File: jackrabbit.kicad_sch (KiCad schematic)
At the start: 55 parts, among them J1 USB_C, J2 PinHeader_2.54mm_02x08, J3 PinHeader_2.54mm_02x08, J4 PinHeader_2.54mm_02x04, J5 PinHeader_2.54mm_02x04, J6 PinHeader_2.54mm_01x04, J7 PinHeader_2.54mm_01x03, SW1 SW_Push, SW2 SW_Push, U1 MIC5319-3.3YD5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

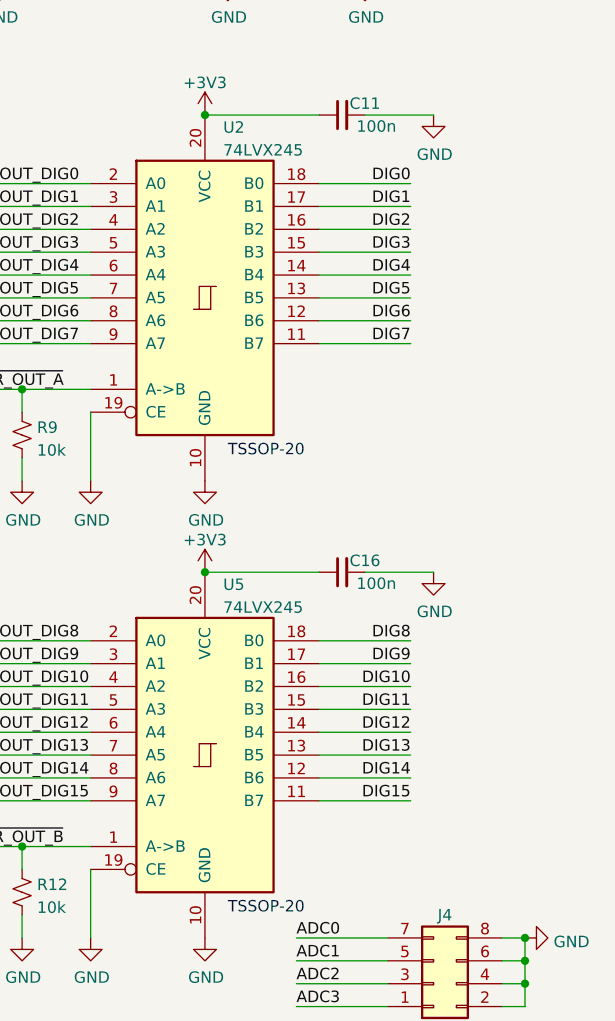
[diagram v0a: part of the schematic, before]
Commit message: Add bus contention series protection resistors
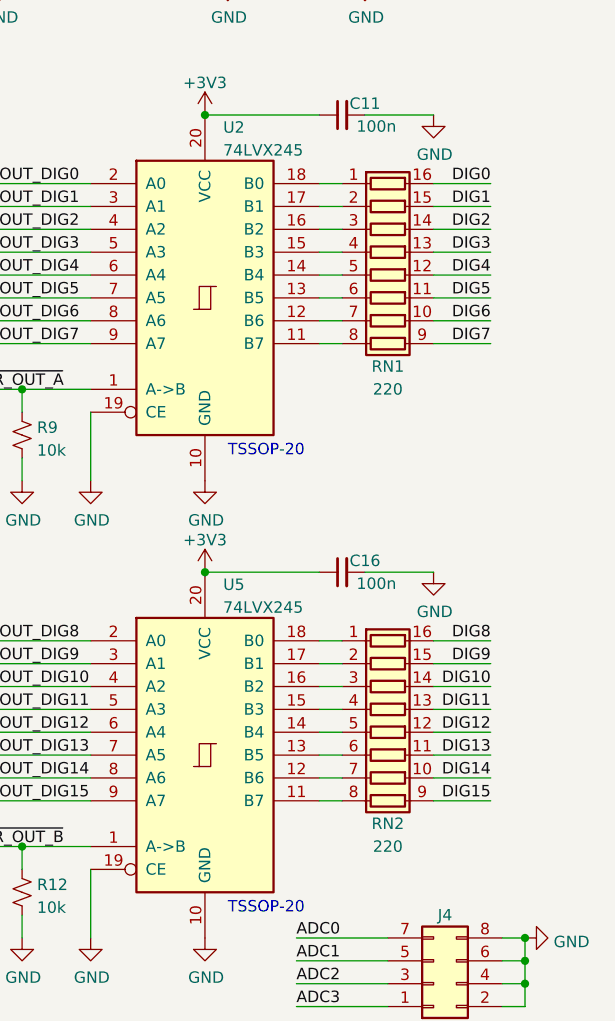
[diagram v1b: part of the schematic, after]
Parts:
- added RN1, RN2: 220, Resistor_SMD:R_Array_Convex_8x0602, symbol Device:R_Pack08
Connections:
- net DIG0: now also RN1.16 (R1.2); no longer U2.18 (B0)
- net DIG1: now also RN1.15 (R2.2); no longer U2.17 (B1)
- net DIG10: now also RN2.14 (R3.2); no longer U5.16 (B2)
- net DIG11: now also RN2.13 (R4.2); no longer U5.15 (B3)
- net DIG12: now also RN2.12 (R5.2); no longer U5.14 (B4)
- net DIG13: now also RN2.11 (R6.2); no longer U5.13 (B5)
- net DIG14: now also RN2.10 (R7.2); no longer U5.12 (B6)
- net DIG15: now also RN2.9 (R8.2); no longer U5.11 (B7)
- net DIG2: now also RN1.14 (R3.2); no longer U2.16 (B2)
- net DIG3: now also RN1.13 (R4.2); no longer U2.15 (B3)
- net DIG4: now also RN1.12 (R5.2); no longer U2.14 (B4)
- net DIG5: now also RN1.11 (R6.2); no longer U2.13 (B5)
- net DIG6: now also RN1.10 (R7.2); no longer U2.12 (B6)
- net DIG7: now also RN1.9 (R8.2); no longer U2.11 (B7)
- net DIG8: now also RN2.16 (R1.2); no longer U5.18 (B0)
- net DIG9: now also RN2.15 (R2.2); no longer U5.17 (B1)
- new net: RN1.8 (R8.1), U2.11 (B7)
- new net: RN1.7 (R7.1), U2.12 (B6)
- new net: RN1.6 (R6.1), U2.13 (B5)
- new net: RN1.5 (R5.1), U2.14 (B4)
- new net: RN1.4 (R4.1), U2.15 (B3)
- new net: RN1.3 (R3.1), U2.16 (B2)
- new net: RN1.2 (R2.1), U2.17 (B1)
- new net: RN1.1 (R1.1), U2.18 (B0)
- new net: RN2.8 (R8.1), U5.11 (B7)
- new net: RN2.7 (R7.1), U5.12 (B6)
- new net: RN2.6 (R6.1), U5.13 (B5)
- new net: RN2.5 (R5.1), U5.14 (B4)
- new net: RN2.4 (R4.1), U5.15 (B3)
- new net: RN2.3 (R3.1), U5.16 (B2)
- new net: RN2.2 (R2.1), U5.17 (B1)
- new net: RN2.1 (R1.1), U5.18 (B0)

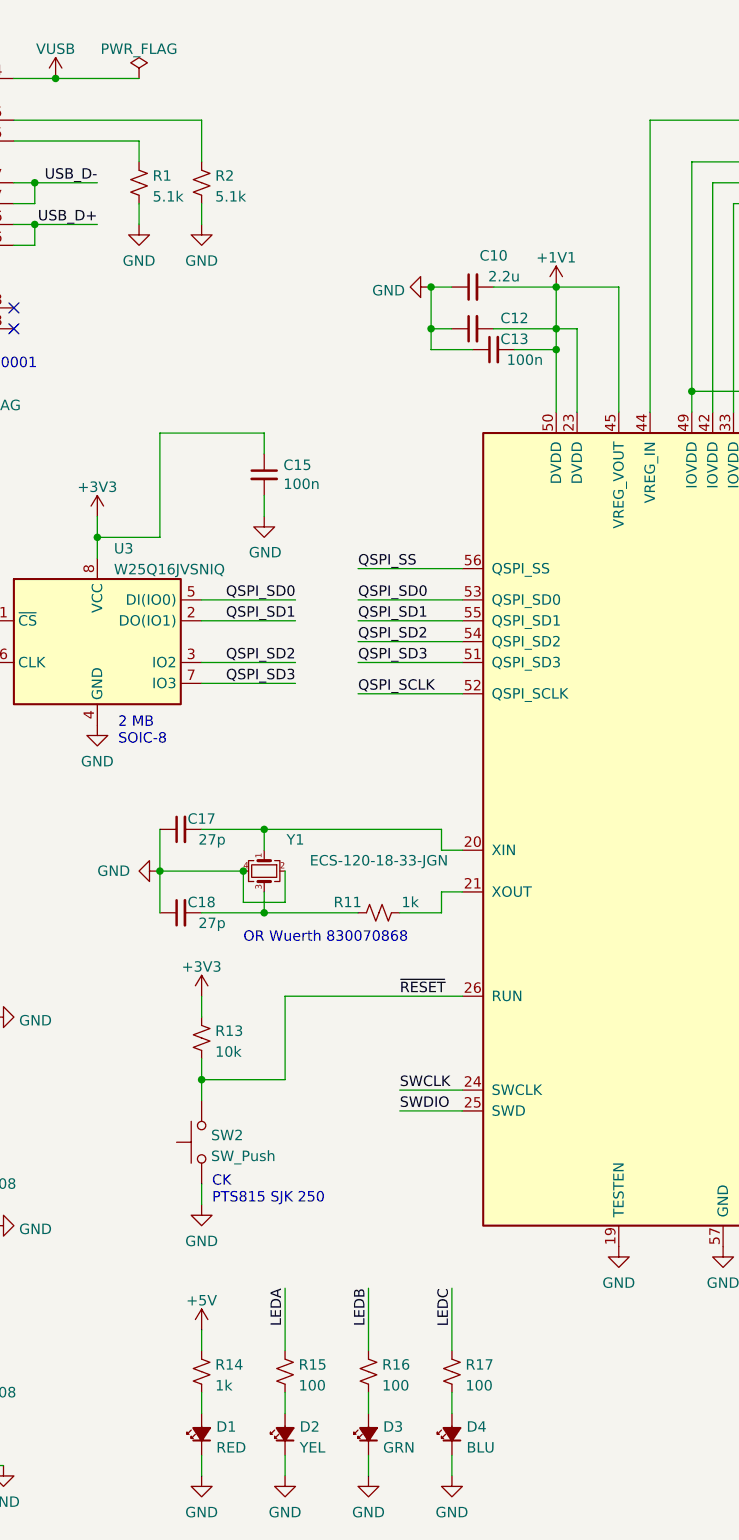
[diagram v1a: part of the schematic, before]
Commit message: Start layout with passives on bottom
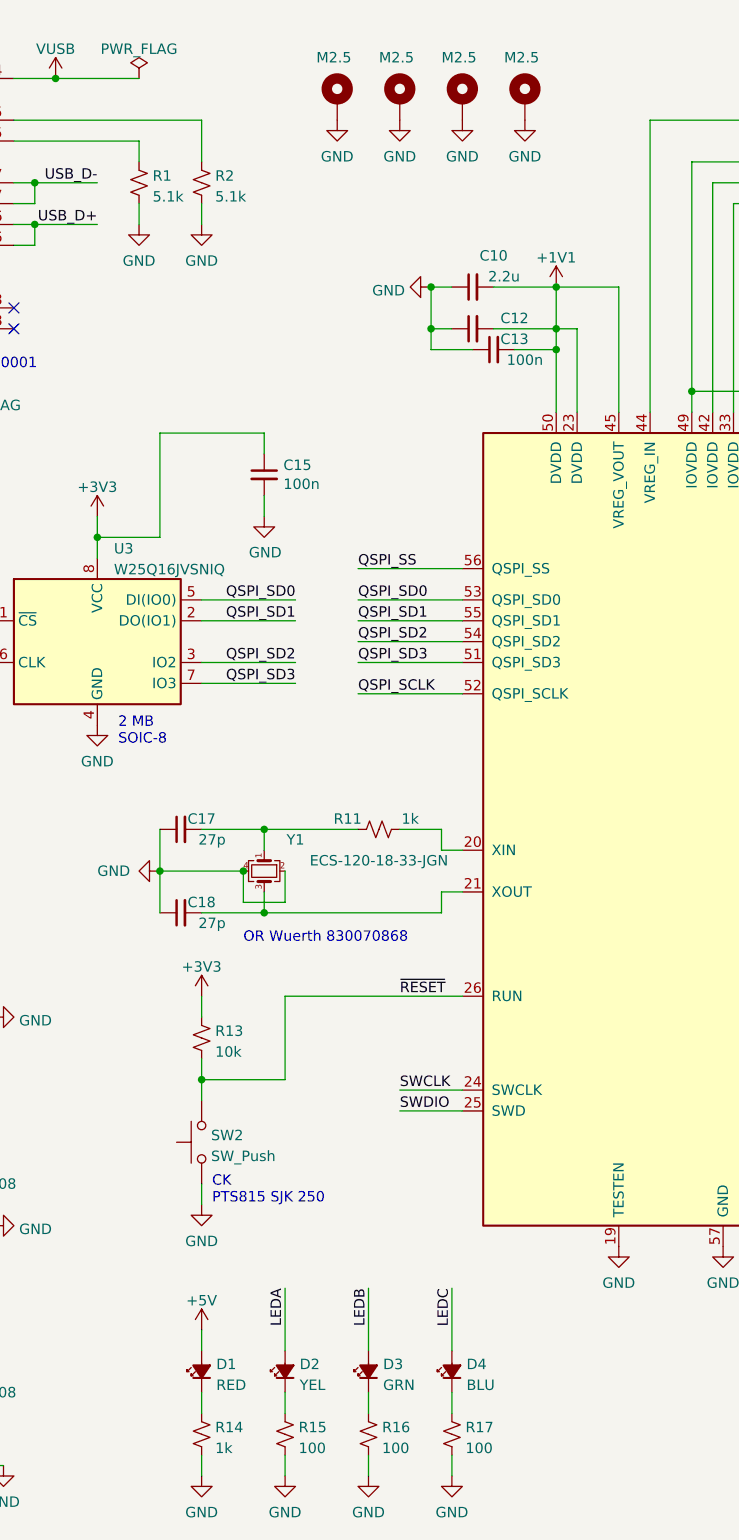
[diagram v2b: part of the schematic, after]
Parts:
- added H1, H2, H3, H4: M2.5, MountingHole:MountingHole_2.7mm_M2.5_Pad_Via, symbol Mechanical:MountingHole_Pad
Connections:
- net +5V: now also D1.2 (A); no longer R14.1
- net GND: now also R14.2, R15.2, R16.2, R17.2, H1.1, H2.1, H3.1, H4.1; no longer D1.1 (K), D2.1 (K), D3.1 (K), D4.1 (K)
- net LEDA: now also D2.2 (A); no longer R15.1
- net LEDB: now also D3.2 (A); no longer R16.1
- net LEDC: now also D4.2 (A); no longer R17.1
- net at C17.2, Y1.1: now also R11.1; no longer U4.20 (XIN)
- net at C18.2, Y1.3: now also U4.21 (XOUT); no longer R11.1
- net at R11.2: now also U4.20 (XIN); no longer U4.21 (XOUT)
- new net: D3.1 (K), R16.1
- new net: D1.1 (K), R14.1
- new net: D2.1 (K), R15.1
- new net: D4.1 (K), R17.1
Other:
- moved on the sheet: D1, D2, D3, D4, R11, R14, R15, R16, R17

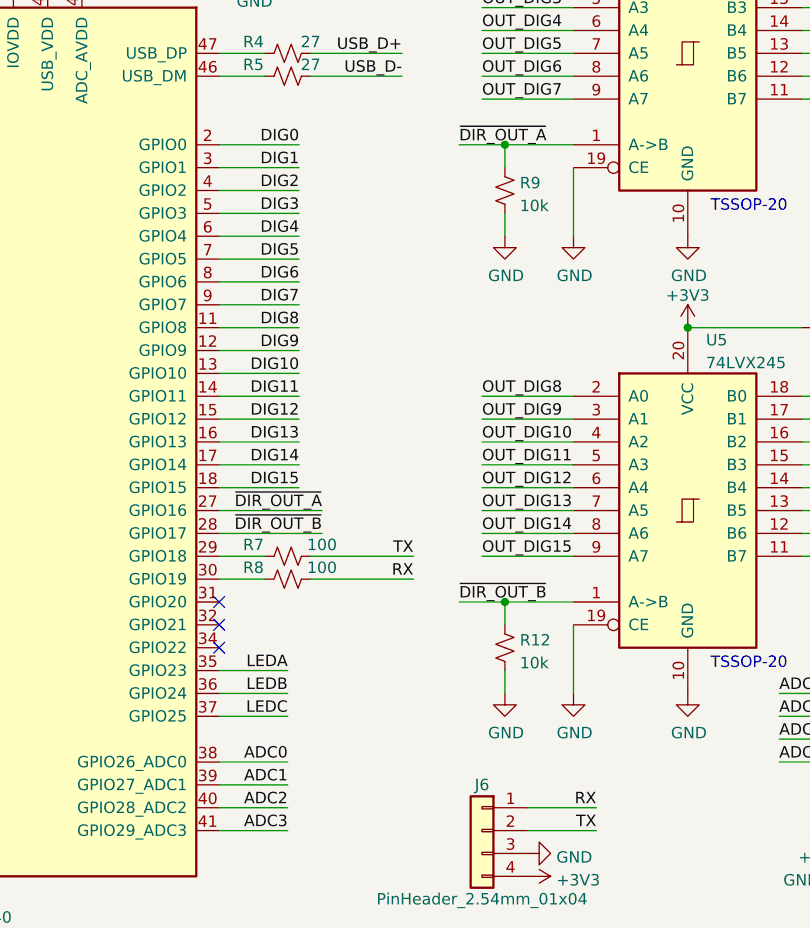
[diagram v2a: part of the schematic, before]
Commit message: Add pullups to disable buffers on power-on
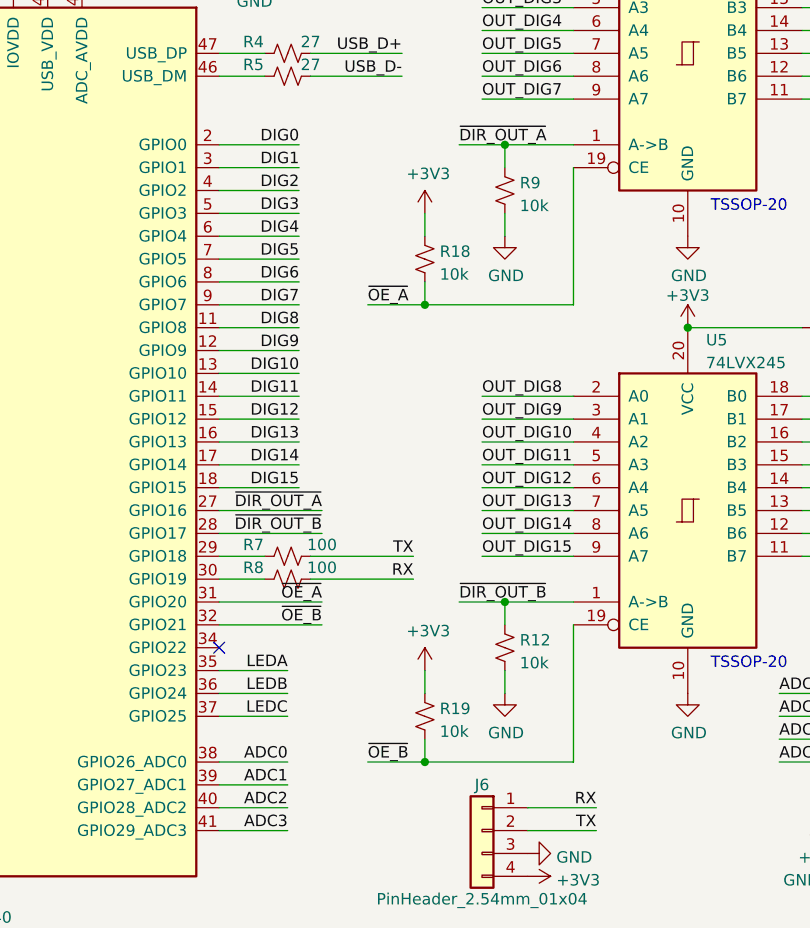
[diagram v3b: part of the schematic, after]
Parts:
- added R18, R19: 10k, Resistor_SMD:R_0603_1608Metric_Pad0.98x0.95mm_HandSolder, symbol Device:R_Small_US
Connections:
- net +3V3: now also R18.1, R19.1
- net GND: no longer U2.19 (CE), U5.19 (CE)
- net ~{OE_A}: now reaches U4.31 (GPIO20)
- net ~{OE_A}: now also U2.19 (CE), R18.2
- net ~{OE_B}: now reaches U4.32 (GPIO21)
- net ~{OE_B}: now also U5.19 (CE), R19.2
- no-connect marks 5 -> 3

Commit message: Redo placement to put USB and digital connector on long axis
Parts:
- removed J3: PinHeader_2.54mm_02x08, Connector_PinHeader_2.54mm:PinHeader_2x08_P2.54mm_Horizontal, symbol Connector_Generic:Conn_02x08_Odd_Even
- J2: value PinHeader_2.54mm_02x08 -> PinHeader_2.54mm_02x10; footprint Connector_PinHeader_2.54mm:PinHeader_2x08_P2.54mm_Horizontal -> Connector_PinHeader_2.54mm:PinHeader_2x10_P2.54mm_Horizontal; symbol Connector_Generic:Conn_02x08_Odd_Even -> Connector_Generic:Conn_02x10_Odd_Even
- renumbered J4 to J3, J5 to J4, J6 to J5, J7 to J6
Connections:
- net +3V3: now also R12.2, R9.2
- net ADC0: no longer J3.7 (Pin_7)
- net DIG0: now also RN1.8 (R8.1); no longer RN1.16 (R1.2)
- net DIG1: now also RN1.7 (R7.1); no longer RN1.15 (R2.2)
- net DIG10: now also RN2.6 (R6.1); no longer RN2.14 (R3.2)
- net DIG11: now also RN2.5 (R5.1); no longer RN2.13 (R4.2)
- net DIG12: now also RN2.4 (R4.1); no longer RN2.12 (R5.2)
- net DIG13: now also RN2.3 (R3.1); no longer RN2.11 (R6.2)
- net DIG14: now also RN2.2 (R2.1); no longer RN2.10 (R7.2)
- net DIG15: now also RN2.1 (R1.1); no longer RN2.9 (R8.2)
- net DIG2: now also RN1.6 (R6.1); no longer RN1.14 (R3.2)
- net DIG3: now also RN1.5 (R5.1); no longer RN1.13 (R4.2)
- net DIG4: now also RN1.4 (R4.1); no longer RN1.12 (R5.2)
- net DIG5: now also RN1.3 (R3.1); no longer RN1.11 (R6.2)
- net DIG6: now also RN1.2 (R2.1); no longer RN1.10 (R7.2)
- net DIG7: now also RN1.1 (R1.1); no longer RN1.9 (R8.2)
- net DIG8: now also RN2.8 (R8.1); no longer RN2.16 (R1.2)
- net DIG9: now also RN2.7 (R7.1); no longer RN2.15 (R2.2)
- net GND: now also J2.1 (Pin_1), J2.19 (Pin_19), J2.20 (Pin_20); no longer J2.10 (Pin_10), J2.12 (Pin_12), J2.14 (Pin_14), J2.16 (Pin_16), J2.4 (Pin_4), J2.6 (Pin_6), J2.8 (Pin_8), R12.2, R9.2
- net OUT_DIG0: now also J2.17 (Pin_17), U2.11 (B7); no longer J2.15 (Pin_15), U2.2 (A0)
- net OUT_DIG1: now also J2.18 (Pin_18), U2.12 (B6); no longer J2.13 (Pin_13), U2.3 (A1)
- net OUT_DIG10: now also J2.7 (Pin_7), U5.13 (B5); no longer U5.4 (A2)
- net OUT_DIG11: now also J2.8 (Pin_8), U5.14 (B4); no longer U5.5 (A3)
- net OUT_DIG12: now also J2.5 (Pin_5), U5.15 (B3); no longer U5.6 (A4)
- net OUT_DIG13: now also J2.6 (Pin_6), U5.16 (B2); no longer U5.7 (A5)
- net OUT_DIG14: now also J2.3 (Pin_3), U5.17 (B1); no longer U5.8 (A6)
- net OUT_DIG15: now also J2.4 (Pin_4), U5.18 (B0); no longer U5.9 (A7)
- net OUT_DIG2: now also J2.15 (Pin_15), U2.13 (B5); no longer J2.11 (Pin_11), U2.4 (A2)
- net OUT_DIG3: now also J2.16 (Pin_16), U2.14 (B4); no longer J2.9 (Pin_9), U2.5 (A3)
- net OUT_DIG4: now also J2.13 (Pin_13), U2.15 (B3); no longer J2.7 (Pin_7), U2.6 (A4)
- net OUT_DIG5: now also J2.14 (Pin_14), U2.16 (B2); no longer J2.5 (Pin_5), U2.7 (A5)
- net OUT_DIG6: now also J2.11 (Pin_11), U2.17 (B1); no longer J2.3 (Pin_3), U2.8 (A6)
- net OUT_DIG7: now also J2.12 (Pin_12), U2.18 (B0); no longer J2.1 (Pin_1), U2.9 (A7)
- net OUT_DIG8: now also J2.9 (Pin_9), U5.11 (B7); no longer U5.2 (A0)
- net OUT_DIG9: now also J2.10 (Pin_10), U5.12 (B6); no longer U5.3 (A1)
- new net: RN1.16 (R1.2), U2.2 (A0)
- new net: RN1.15 (R2.2), U2.3 (A1)
- new net: RN1.14 (R3.2), U2.4 (A2)
- new net: RN1.13 (R4.2), U2.5 (A3)
- new net: RN1.12 (R5.2), U2.6 (A4)
- new net: RN1.11 (R6.2), U2.7 (A5)
- new net: RN1.10 (R7.2), U2.8 (A6)
- new net: RN1.9 (R8.2), U2.9 (A7)
- new net: RN2.16 (R1.2), U5.2 (A0)
- new net: RN2.15 (R2.2), U5.3 (A1)
- new net: RN2.14 (R3.2), U5.4 (A2)
- new net: RN2.13 (R4.2), U5.5 (A3)
- new net: RN2.12 (R5.2), U5.6 (A4)
- new net: RN2.11 (R6.2), U5.7 (A5)
- new net: RN2.10 (R7.2), U5.8 (A6)
- new net: RN2.9 (R8.2), U5.9 (A7)
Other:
- note removed: "OR Wuerth 434133025816"
- note removed: "OR Wuerth 830070868"
- moved on the sheet: C11, C16, J3, J4, J5, R12, R18, R19, R9, RN1, RN2, U2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

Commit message: Change footprints to those of ordered parts
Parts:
- J1: footprint jackrabbit:USB_C_Receptacle_Molex_2171790001 -> jackrabbit:USB_C_Receptacle_GCT_USB4105-GF-A-120
- SW1, SW2: footprint Button_Switch_SMD:SW_Push_1P1T_NO_Vertical_Wuerth_434133025816 -> jackrabbit:SW_Push_CK_PTS815_HandSoldering
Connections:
- net GND: no longer J1.S1 (SHIELD)
- no-connect marks 3 -> 4
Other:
- note added: "GCT USB4105-GF-A-120"
- note removed: "Molex 2171790001"
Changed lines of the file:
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@@
   (no_connect (at 166.37 137.16))
   (no_connect (at 48.26 50.8))
+  (no_connect (at 25.4 60.96))
   (no_connect (at 48.26 53.34))
   (wire (pts (xy 228.6 25.4) (xy 236.22 25.4))
@@
     (effects (font (size 1.27 1.27)) (justify left bottom))
   )
-  (text "Molex 2171790001" (at 34.29 58.42 0)
+  (text "GCT USB4105-GF-A-120 " (at 34.29 58.42 0)
     (effects (font (size 1.27 1.27)) (justify left bottom))
   )
@@
     (pin "1")
   )
-  (symbol (lib_id "power:GND") (at 25.4 60.96 0) (unit 1)
-    (in_bom yes) (on_board yes) (fields_autoplaced)
-    (property "Reference" "#PWR017" (id 0) (at 25.4 67.31 0)
-      (effects (font (size 1.27 1.27)) hide)
-    )
-    (property "Value" "GND" (id 1) (at 25.4 65.4034 0))
-    (property "Footprint" "" (id 2) (at 25.4 60.96 0)
-      (effects (font (size 1.27 1.27)) hide)
-    )
-    (property "Datasheet" "" (id 3) (at 25.4 60.96 0)
-      (effects (font (size 1.27 1.27)) hide)
-    )
-    (pin "1")
-  )
   (symbol (lib_id "power:GND") (at 63.5 40.64 0) (unit 1)
     (in_bom yes) (on_board yes) (fields_autoplaced)
@@
       (effects (font (size 1.27 1.27)) (justify right))
     )
-    (property "Footprint" "Button_Switch_SMD:SW_Push_1P1T_NO_Vertical_Wuerth_434133025816" (id 2) (at 25.4 116.84 0)
+    (property "Footprint" "jackrabbit:SW_Push_CK_PTS815_HandSoldering" (id 2) (at 25.4 116.84 0)
       (effects (font (size 1.27 1.27)) hide)
     )
-    (property "Datasheet" "https://www.mouser.com/datasheet/2/445/434133025816-2889591.pdf" (id 3) (at 25.4 116.84 0)
+    (property "Datasheet" "https://www.ckswitches.com/media/2728/pts815.pdf" (id 3) (at 25.4 116.84 0)
       (effects (font (size 1.27 1.27)) hide)
     )
@@
     (property "Reference" "J1" (id 0) (at 33.02 16.6202 0))
     (property "Value" "USB_C" (id 1) (at 33.02 19.1571 0))
-    (property "Footprint" "jackrabbit:USB_C_Receptacle_Molex_2171790001" (id 2) (at 36.83 38.1 0)
+    (property "Footprint" "jackrabbit:USB_C_Receptacle_GCT_USB4105-GF-A-120" (id 2) (at 36.83 38.1 0)
       (effects (font (size 1.27 1.27)) hide)
     )
-    (property "Datasheet" "https://www.molex.com/pdm_docs/sd/2171790001_sd.pdf" (id 3) (at 36.83 38.1 0)
+    (property "Datasheet" "https://www.mouser.com/datasheet/2/837/usb4105-2448855.pdf" (id 3) (at 36.83 38.1 0)
       (effects (font (size 1.27 1.27)) hide)
     )
@@
       (effects (font (size 1.27 1.27)) (justify right))
     )
-    (property "Footprint" "Button_Switch_SMD:SW_Push_1P1T_NO_Vertical_Wuerth_434133025816" (id 2) (at 66.04 152.4 0)
+    (property "Footprint" "jackrabbit:SW_Push_CK_PTS815_HandSoldering" (id 2) (at 66.04 152.4 0)
       (effects (font (size 1.27 1.27)) hide)
     )
-    (property "Datasheet" "https://www.mouser.com/datasheet/2/445/434133025816-2889591.pdf" (id 3) (at 66.04 152.4 0)
+    (property "Datasheet" "https://www.ckswitches.com/media/2728/pts815.pdf" (id 3) (at 66.04 152.4 0)
       (effects (font (size 1.27 1.27)) hide)
     )
@@
       (reference "#PWR016") (unit 1) (value "GND") (footprint "")
     )
-    (path "/28f2707c-4b52-4699-b167-fc14e4ee7daf"
-      (reference "#PWR017") (unit 1) (value "GND") (footprint "")
-    )
     (path "/1033899b-bab1-48ed-9836-4ce8113a7185"
       (reference "#PWR018") (unit 1) (value "GND") (footprint "")
@@
     )
     (path "/ac3dcbf8-e9e2-4607-b118-36dab8841ac1"
-      (reference "J1") (unit 1) (value "USB_C") (footprint "jackrabbit:USB_C_Receptacle_Molex_2171790001")
+      (reference "J1") (unit 1) (value "USB_C") (footprint "jackrabbit:USB_C_Receptacle_GCT_USB4105-GF-A-120")
     )
     (path "/791214ba-3f08-4a8f-b2f1-03e7cde5a47c"
@@
     )
     (path "/75168e4c-e04a-4b5e-b9ee-5dd3360eff4e"
-      (reference "SW1") (unit 1) (value "SW_Push") (footprint "Button_Switch_SMD:SW_Push_1P1T_NO_Vertical_Wuerth_434133025816")
+      (reference "SW1") (unit 1) (value "SW_Push") (footprint "jackrabbit:SW_Push_CK_PTS815_HandSoldering")
     )
     (path "/de0afef4-6721-455b-88fc-146d95ed561d"
-      (reference "SW2") (unit 1) (value "SW_Push") (footprint "Button_Switch_SMD:SW_Push_1P1T_NO_Vertical_Wuerth_434133025816")
+      (reference "SW2") (unit 1) (value "SW_Push") (footprint "jackrabbit:SW_Push_CK_PTS815_HandSoldering")
     )
     (path "/f81ff424-0e89-4d04-a430-947d7766c60a"
